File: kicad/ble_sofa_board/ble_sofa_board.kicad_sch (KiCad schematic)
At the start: 17 parts, among them J1 Screw_Terminal_01x02, J2 Screw_Terminal_01x02, J5 Screw_Terminal_01x02, J6 Screw_Terminal_01x02, J7 RJ9, U1 LM2596S_Buck_Module, U3 Pico_Dual_Channel_Relay_HAT

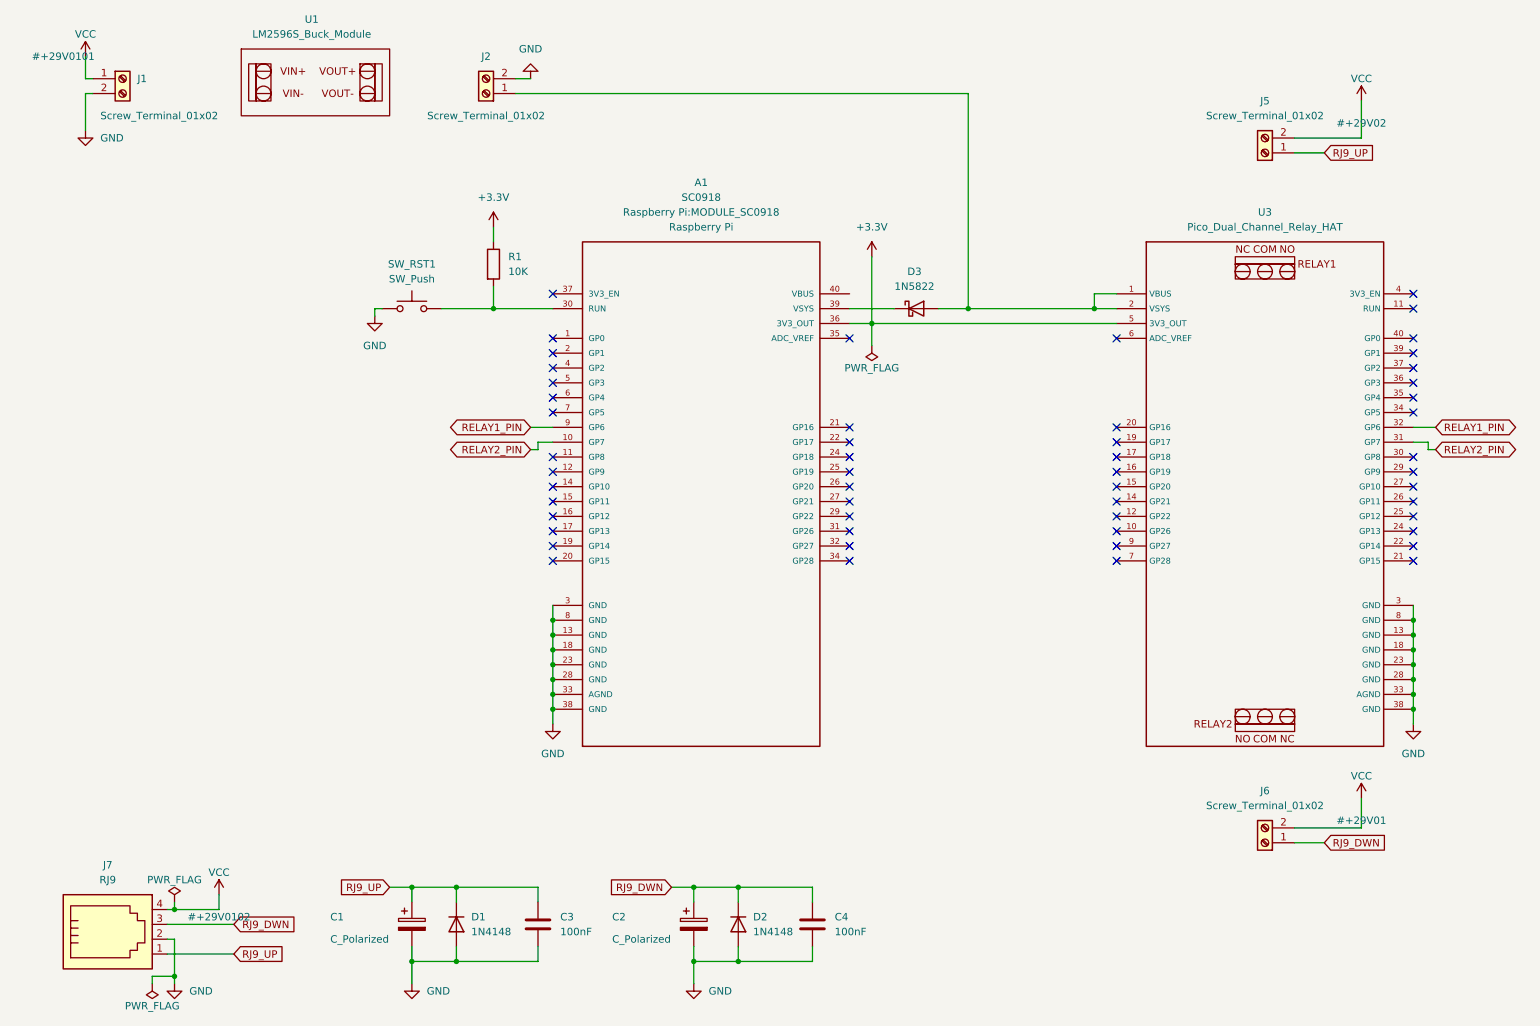
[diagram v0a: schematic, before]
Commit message: ble_sofa - pcb - Update schematics with soft start circuit and OLED display
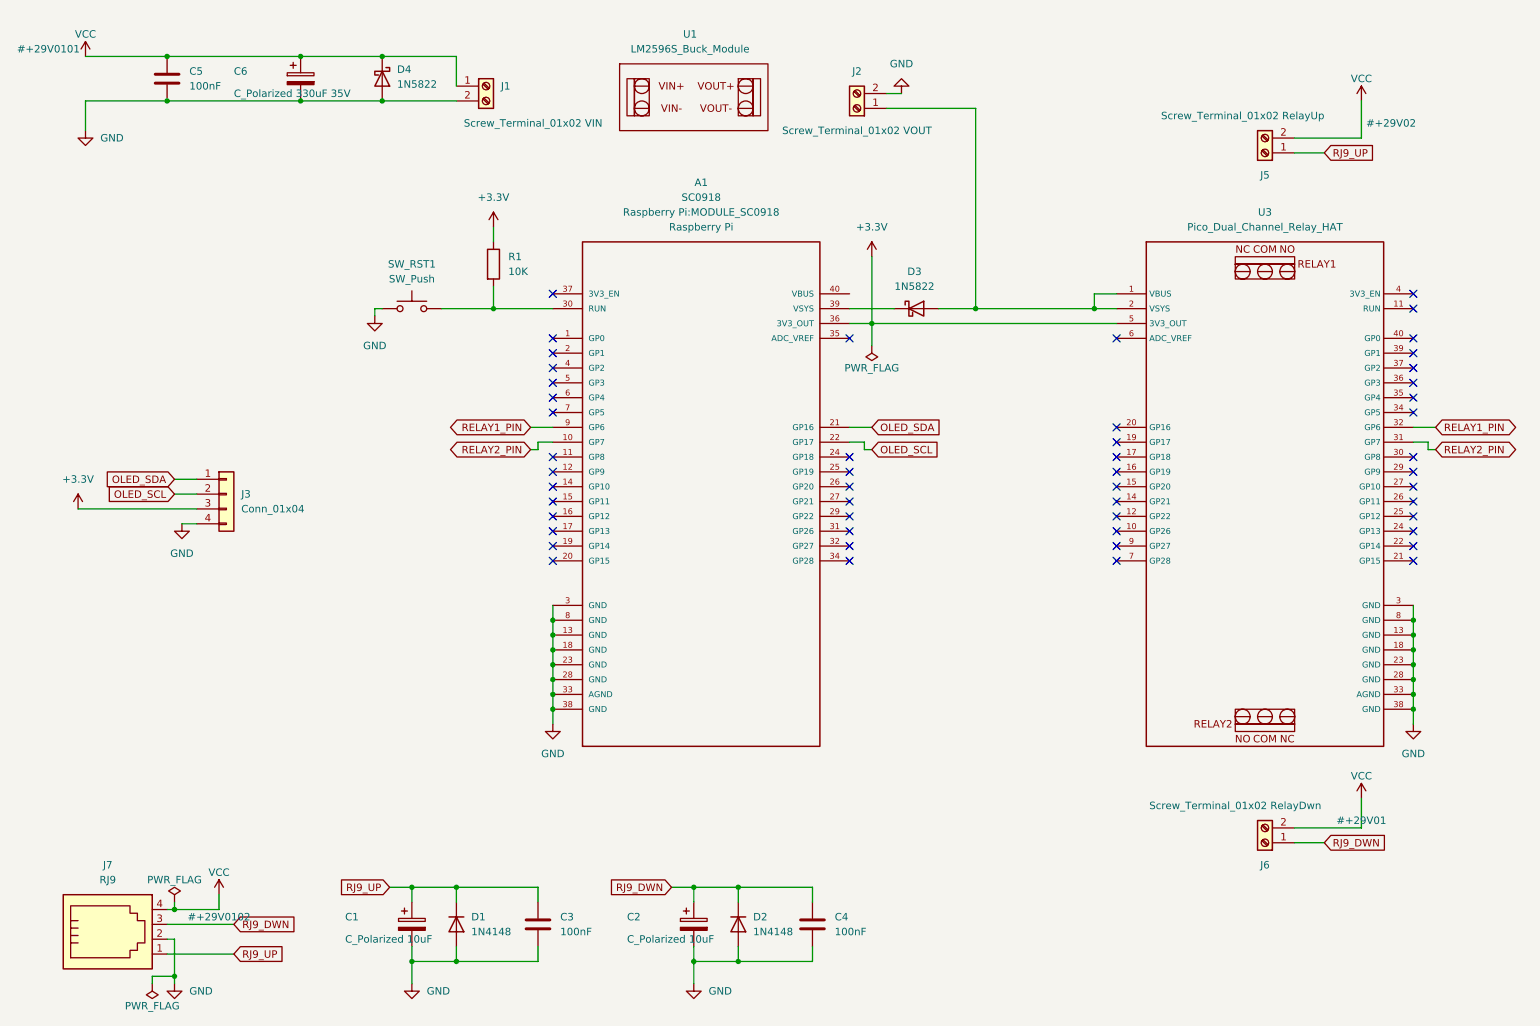
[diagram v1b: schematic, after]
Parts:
- added C5: 100nF, symbol Device:C
- added C6: C_Polarized 330uF 35V, Capacitor_THT:CP_Radial_D5.0mm_P2.50mm, symbol Device:C_Polarized
- added D4: 1N5822, Diode_THT:D_DO-201AD_P15.24mm_Horizontal, symbol Diode:1N5822
- added J3: Conn_01x04, Connector_PinHeader_2.54mm:PinHeader_1x04_P2.54mm_Vertical, symbol Connector_Generic:Conn_01x04
- C1, C2: value C_Polarized -> C_Polarized 10uF
- J1: value Screw_Terminal_01x02 -> Screw_Terminal_01x02 VIN
- J2: value Screw_Terminal_01x02 -> Screw_Terminal_01x02 VOUT
- J5: value Screw_Terminal_01x02 -> Screw_Terminal_01x02 RelayUp
- J6: value Screw_Terminal_01x02 -> Screw_Terminal_01x02 RelayDwn
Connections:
- net +3.3V: now also J3.3 (Pin_3)
- net GND: now also C5.2, C6.2, D4.2 (A), J3.4 (Pin_4)
- net VCC: now also C5.1, C6.1, D4.1 (K)
- net OLED_SDA: now reaches A1.21 (GP16)
- net OLED_SDA: now also J3.1 (Pin_1)
- net OLED_SCL: now reaches A1.22 (GP17)
- net OLED_SCL: now also J3.2 (Pin_2)
- no-connect marks 53 -> 51
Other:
- moved on the sheet: J1, J2, U1

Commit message: ble_sofa - Update PCB layout
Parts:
- A1: footprint Raspberry Pi:MODULE_SC0918 -> Raspberry_Pi_Pico_W_SC0918:MODULE_SC0918
- C1, C2: footprint Capacitor_THT:CP_Radial_D5.0mm_P2.50mm -> Capacitor_THT:CP_Radial_D5.0mm_P2.00mm
- C3, C4, C5: footprint (none) -> Capacitor_THT:C_Disc_D7.0mm_W2.5mm_P5.00mm
- C6: footprint Capacitor_THT:CP_Radial_D5.0mm_P2.50mm -> Capacitor_THT:CP_Radial_D10.0mm_P5.00mm
- J3: footprint Connector_PinHeader_2.54mm:PinHeader_1x04_P2.54mm_Vertical -> SB_Components:OLED_I2C_128x32_SSD1306
- R1: footprint (none) -> Resistor_THT:R_Axial_DIN0207_L6.3mm_D2.5mm_P10.16mm_Horizontal
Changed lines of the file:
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@@
       (effects (font (size 1.27 1.27)) (justify left))
     )
-    (property "Footprint" "" (at 154.6352 172.72 0)
+    (property "Footprint" "Capacitor_THT:C_Disc_D7.0mm_W2.5mm_P5.00mm" (at 154.6352 172.72 0)
       (effects (font (size 1.27 1.27)) hide)
     )
@@
       (effects (font (size 1.27 1.27)) (justify left))
     )
-    (property "Footprint" "" (at 97.282 55.88 90)
+    (property "Footprint" "Resistor_THT:R_Axial_DIN0207_L6.3mm_D2.5mm_P10.16mm_Horizontal" (at 97.282 55.88 90)
       (effects (font (size 1.27 1.27)) hide)
     )
@@
       (effects (font (size 1.27 1.27)))
     )
-    (property "Footprint" "Raspberry Pi:MODULE_SC0918" (at 134.62 46.99 0)
+    (property "Footprint" "Raspberry_Pi_Pico_W_SC0918:MODULE_SC0918" (at 134.62 46.99 0)
       (effects (font (size 1.27 1.27)))
     )
@@
       (effects (font (size 1.27 1.27)) (justify left))
     )
-    (property "Footprint" "Capacitor_THT:CP_Radial_D5.0mm_P2.50mm" (at 86.0552 172.72 0)
+    (property "Footprint" "Capacitor_THT:CP_Radial_D5.0mm_P2.00mm" (at 86.0552 172.72 0)
       (effects (font (size 1.27 1.27)) hide)
     )
@@
       (effects (font (size 1.27 1.27)) (justify left))
     )
-    (property "Footprint" "Capacitor_THT:CP_Radial_D5.0mm_P2.50mm" (at 67.0052 27.94 0)
+    (property "Footprint" "Capacitor_THT:CP_Radial_D10.0mm_P5.00mm" (at 67.0052 27.94 0)
       (effects (font (size 1.27 1.27)) hide)
     )
@@
       (effects (font (size 1.27 1.27)) (justify left))
     )
-    (property "Footprint" "Capacitor_THT:CP_Radial_D5.0mm_P2.50mm" (at 134.3152 172.72 0)
+    (property "Footprint" "Capacitor_THT:CP_Radial_D5.0mm_P2.00mm" (at 134.3152 172.72 0)
       (effects (font (size 1.27 1.27)) hide)
     )
@@
       (effects (font (size 1.27 1.27)) (justify left))
     )
-    (property "Footprint" "" (at 44.1452 27.94 0)
+    (property "Footprint" "Capacitor_THT:C_Disc_D7.0mm_W2.5mm_P5.00mm" (at 44.1452 27.94 0)
       (effects (font (size 1.27 1.27)) hide)
     )
@@
       (effects (font (size 1.27 1.27)) (justify left))
     )
-    (property "Footprint" "Connector_PinHeader_2.54mm:PinHeader_1x04_P2.54mm_Vertical" (at 53.34 95.25 0)
+    (property "Footprint" "SB_Components:OLED_I2C_128x32_SSD1306" (at 53.34 95.25 0)
       (effects (font (size 1.27 1.27)) hide)
     )
@@
       (effects (font (size 1.27 1.27)) (justify left))
     )
-    (property "Footprint" "" (at 107.6452 172.72 0)
-      (effects (font (size 1.27 1.27)) hide)
-    )
+    (property "Footprint" "Capacitor_THT:C_Disc_D7.0mm_W2.5mm_P5.00mm" (at 107.6452 172.72 0)
+      (effects (font (size 1.27 1.27)) hide)
+    )

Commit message: ble_sofa - pcb - WIP routing
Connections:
- net RELAY1_PIN: now also A1.10 (GP7); no longer A1.9 (GP6)
- net RELAY2_PIN: now also A1.9 (GP6); no longer A1.10 (GP7)
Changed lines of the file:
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@@
     )
   )
-  (global_label "RELAY2_PIN" (shape bidirectional) (at 105.41 87.63 180) (fields_autoplaced)
+  (global_label "RELAY1_PIN" (shape bidirectional) (at 105.41 87.63 180) (fields_autoplaced)
     (effects (font (size 1.27 1.27)) (justify right))
-    (property "Intersheetrefs" "${INTERSHEET_REFS}" (at 91.9902 87.5506 0)
+    (property "Intersheetrefs" "${INTERSHEET_REFS}" (at 90.3068 87.63 0)
       (effects (font (size 1.27 1.27)) (justify right) hide)
     )
@@
     )
   )
-  (global_label "RELAY1_PIN" (shape bidirectional) (at 105.41 83.82 180) (fields_autoplaced)
+  (global_label "RELAY2_PIN" (shape bidirectional) (at 105.41 83.82 180) (fields_autoplaced)
     (effects (font (size 1.27 1.27)) (justify right))
-    (property "Intersheetrefs" "${INTERSHEET_REFS}" (at 91.9902 83.7406 0)
+    (property "Intersheetrefs" "${INTERSHEET_REFS}" (at 90.3068 83.82 0)
       (effects (font (size 1.27 1.27)) (justify right) hide)
     )
